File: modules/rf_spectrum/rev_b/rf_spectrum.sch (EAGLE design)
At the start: 45 parts, among them J3 SIGNPOST_DEBUG_HEADERSMT, J4 SIGNPOST_MODULE_HEADER, J5 TC2030-JLINK-L, Q1 SI223DDS, U1 MWSUB3G, U2 SKY13317, U3 STM32L432KC, U4 TLV62130, X1 ABS05-32.768KHZ-T

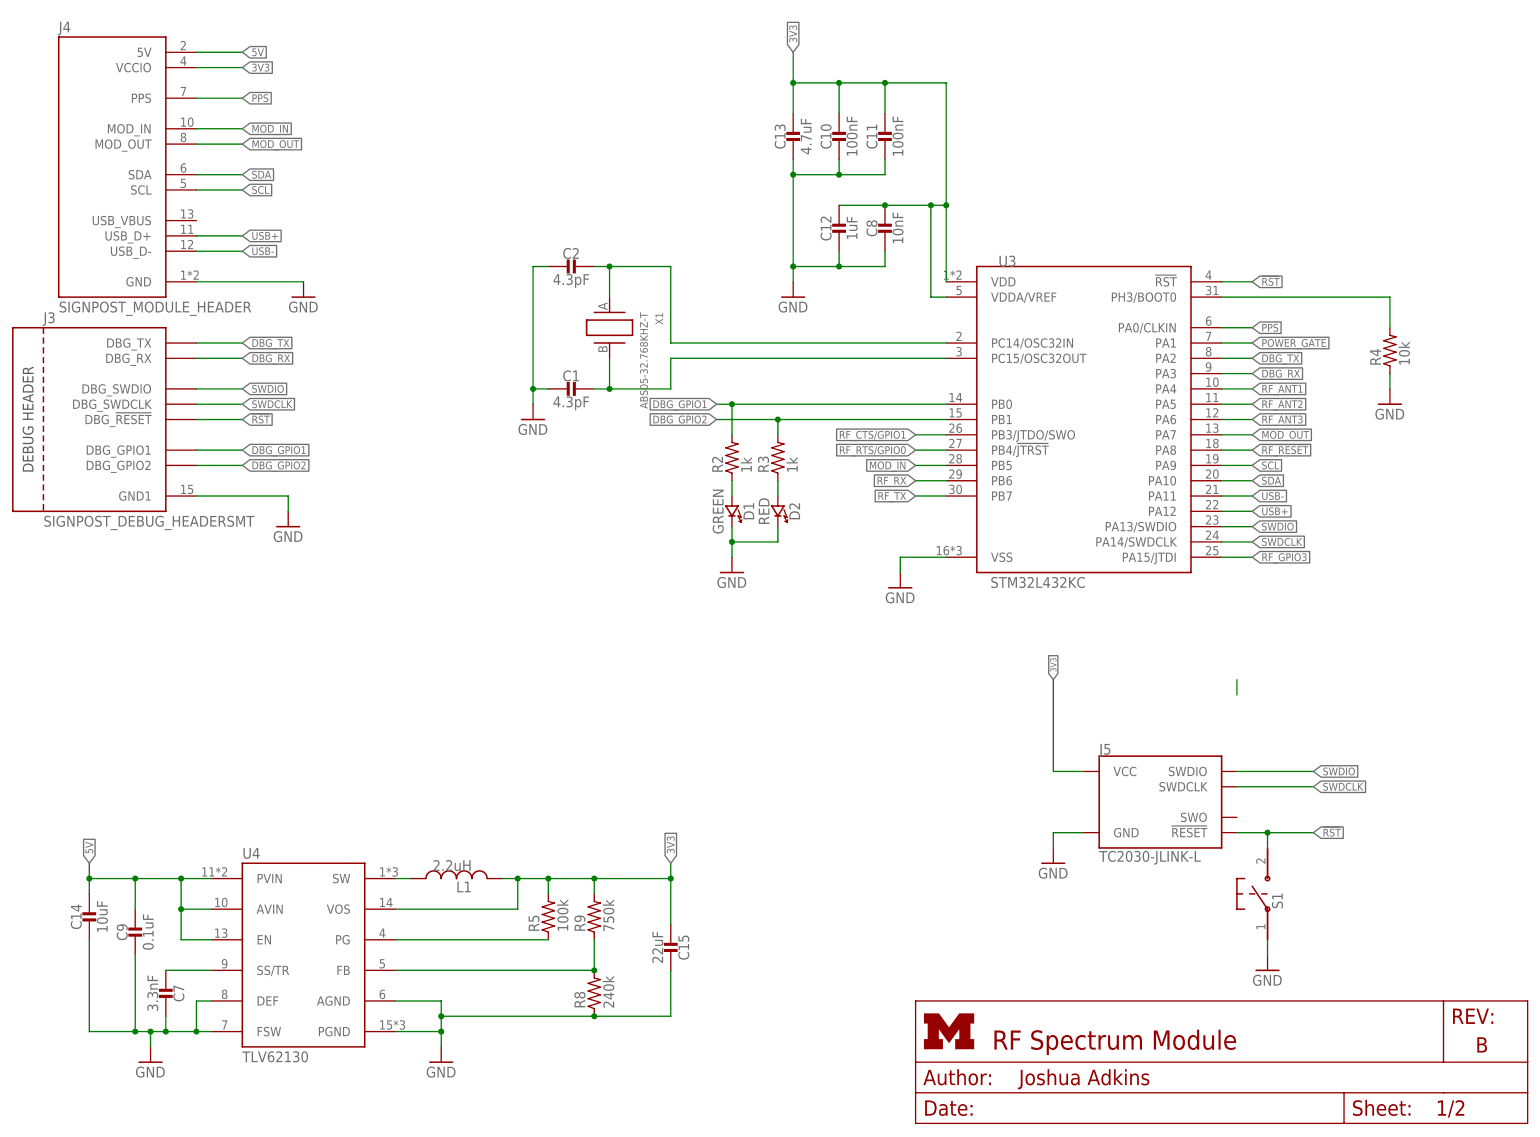
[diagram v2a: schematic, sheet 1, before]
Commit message: renumbered componenets, added BOM
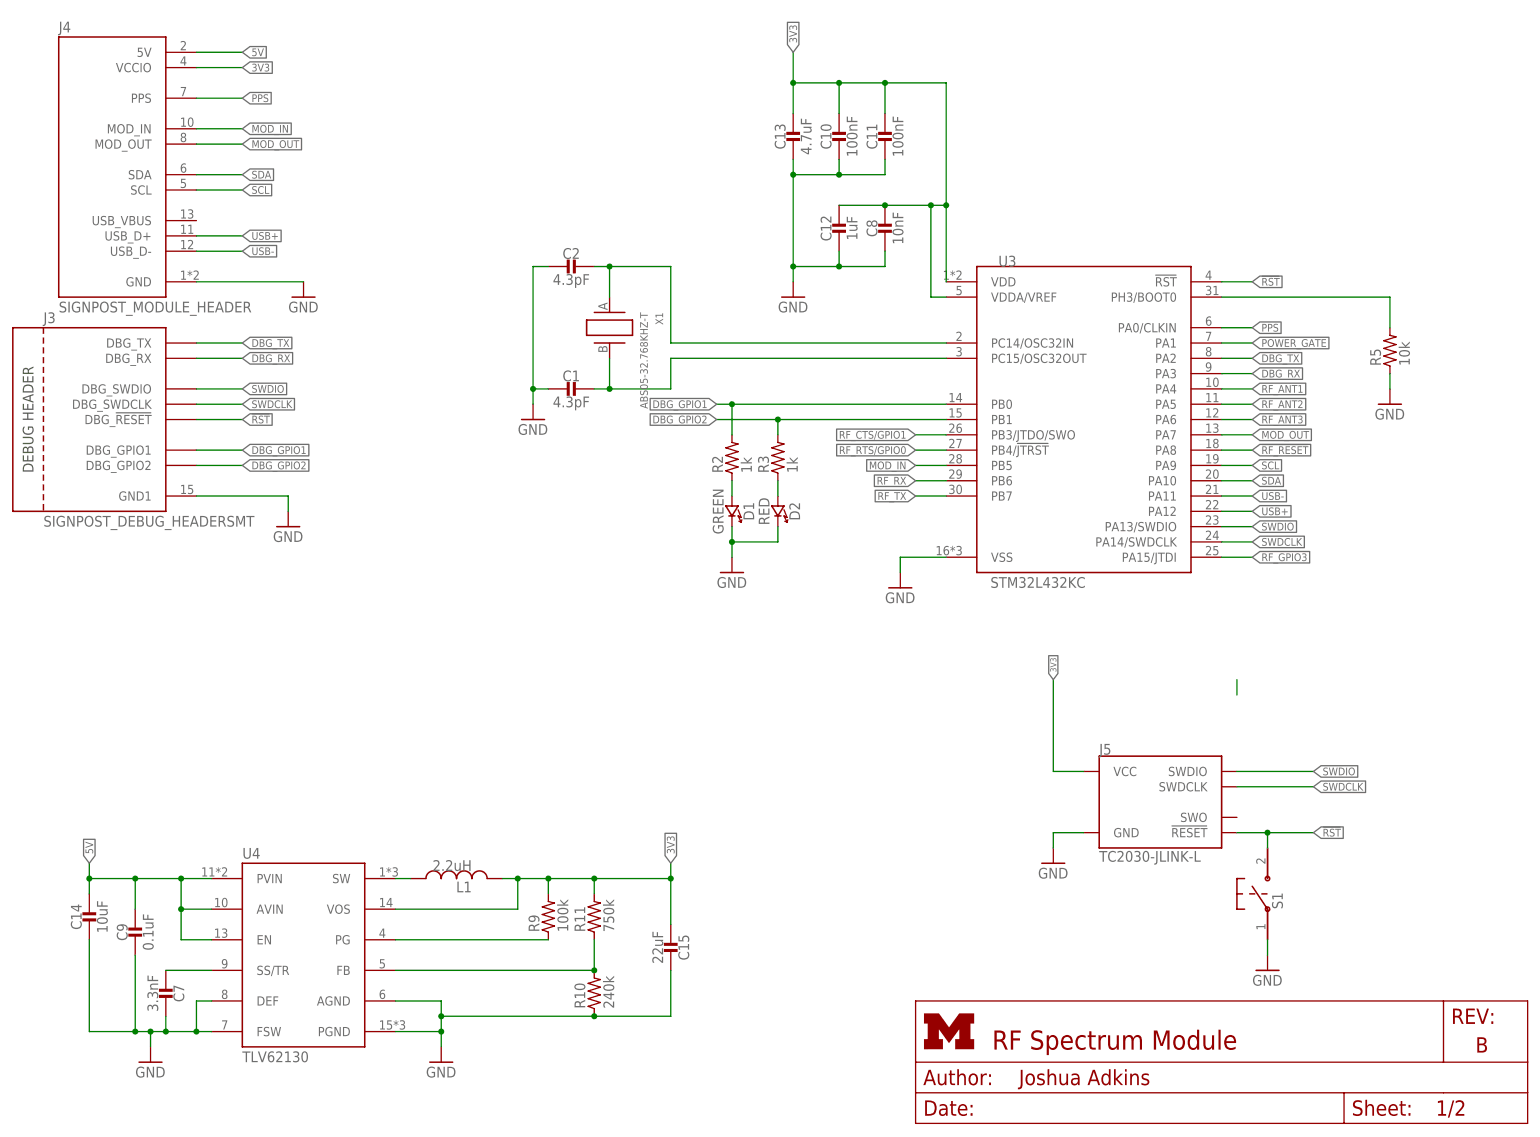
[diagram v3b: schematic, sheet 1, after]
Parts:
- R10: value 1k -> 240k; device passives:RESISTOR0402_RES -> passives:RESISTOR0603_RES; DIGIKEY 311-100KLRCT-ND -> 311-240KGRCT-ND; MPN RC0402FR-07100KL -> RC0603JR-07240KL
- R11: value 100k -> 750k; device passives:RESISTOR0402_RES -> passives:RESISTOR0603_RES; DIGIKEY 311-100KLRCT-ND -> 311-750KGRCT-ND; MPN RC0402FR-07100KL -> 311-750KGRCT-ND
- R4: value 10k -> 1k; DIGIKEY 311-1.0KJRCT-ND -> 311-100KLRCT-ND; MPN RC0402JR-071KL -> RC0402FR-07100KL
- R5: value 100k -> 10k; device passives:RESISTOR0603_RES -> passives:RESISTOR0402_RES; DIGIKEY 311-100KGRCT-ND -> 311-1.0KJRCT-ND; MPN RC0603JR-07100KL -> RC0402JR-071KL
- R8: value 240k -> 100k; device passives:RESISTOR0603_RES -> passives:RESISTOR0402_RES; DIGIKEY 311-240KGRCT-ND -> 311-100KLRCT-ND; MPN RC0603JR-07240KL -> RC0402FR-07100KL
- R9: value 750k -> 100k; DIGIKEY 311-750KGRCT-ND -> 311-100KGRCT-ND; MPN 311-750KGRCT-ND -> RC0603JR-07100KL
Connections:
- net 3V3: now also R11.2, R7.2; no longer R5.2, R6.2
- net GATED: now also R8.1; no longer R11.1
- net GND: now also R10.1, R5.1, R6.2; no longer R4.1, R7.2, R8.1
- net N$11: now also R5.2; no longer R4.2
- net N$13: now also R4.1, R7.1; no longer R10.1, R6.1
- net N$36: now also R9.1; no longer R5.1
- net N$37: now also R10.2, R11.1; no longer R8.2, R9.1
- net POWER_GATE: now also R4.2; no longer R10.2
- net RF_GPIO2: now also R6.1; no longer R7.1
- net RF_GPIO3: now also R8.2; no longer R11.2
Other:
- moved on the sheet: R5, R6, R7, R9

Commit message: fixed BOM line item
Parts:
- R4: DIGIKEY 311-100KLRCT-ND -> 311-1.0KJRCT-ND; MPN RC0402FR-07100KL -> RC0402JR-071KL
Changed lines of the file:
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@@
 </part>
 <part name="R4" library="passives" deviceset="RESISTOR" device="0402_RES" value="1k">
-<attribute name="DIGIKEY" value="311-100KLRCT-ND"/>
+<attribute name="DIGIKEY" value="311-1.0KJRCT-ND"/>
 <attribute name="MANUFACTURER" value="Yageo"/>
-<attribute name="MPN" value="RC0402FR-07100KL"/>
+<attribute name="MPN" value="RC0402JR-071KL"/>
 </part>
 <part name="J4" library="signpost" deviceset="SIGNPOST_MODULE_HEADER" device=""/>
